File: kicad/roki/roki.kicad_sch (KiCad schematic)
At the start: 64 parts, among them SW1 RotaryEncoder_Switch, SW2 SW_SPDT, U1 Nice_Nano_V2

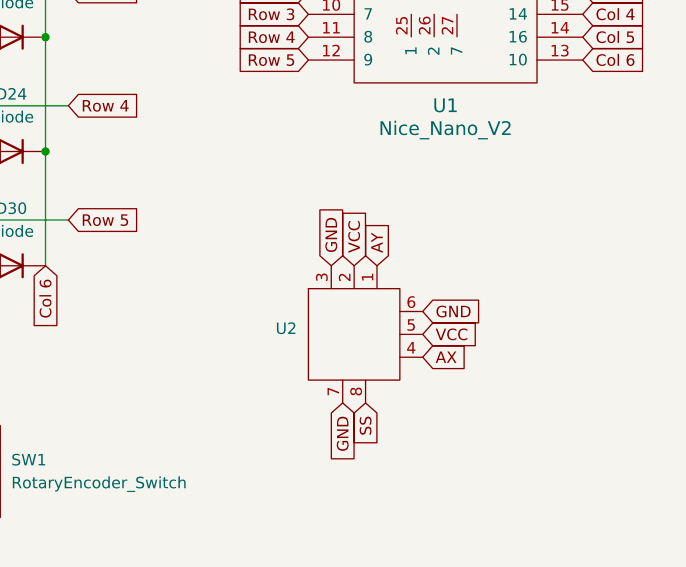
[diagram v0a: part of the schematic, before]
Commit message: fix(kicad): fix thumb stick pin schematics
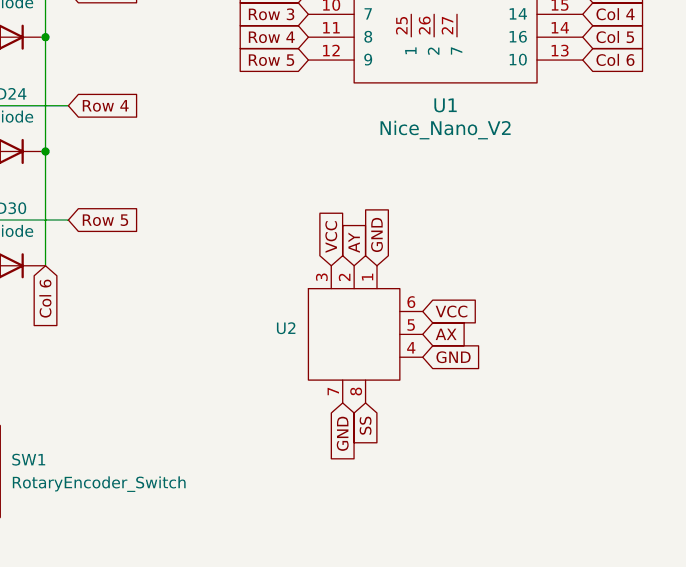
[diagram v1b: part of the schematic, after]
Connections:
- net AX: now also U2.5; no longer U2.4
- net AY: now also U2.2; no longer U2.1
- net GND: now also U2.1, U2.4; no longer U2.3, U2.6
- net VCC: now also U2.3, U2.6; no longer U2.2, U2.5

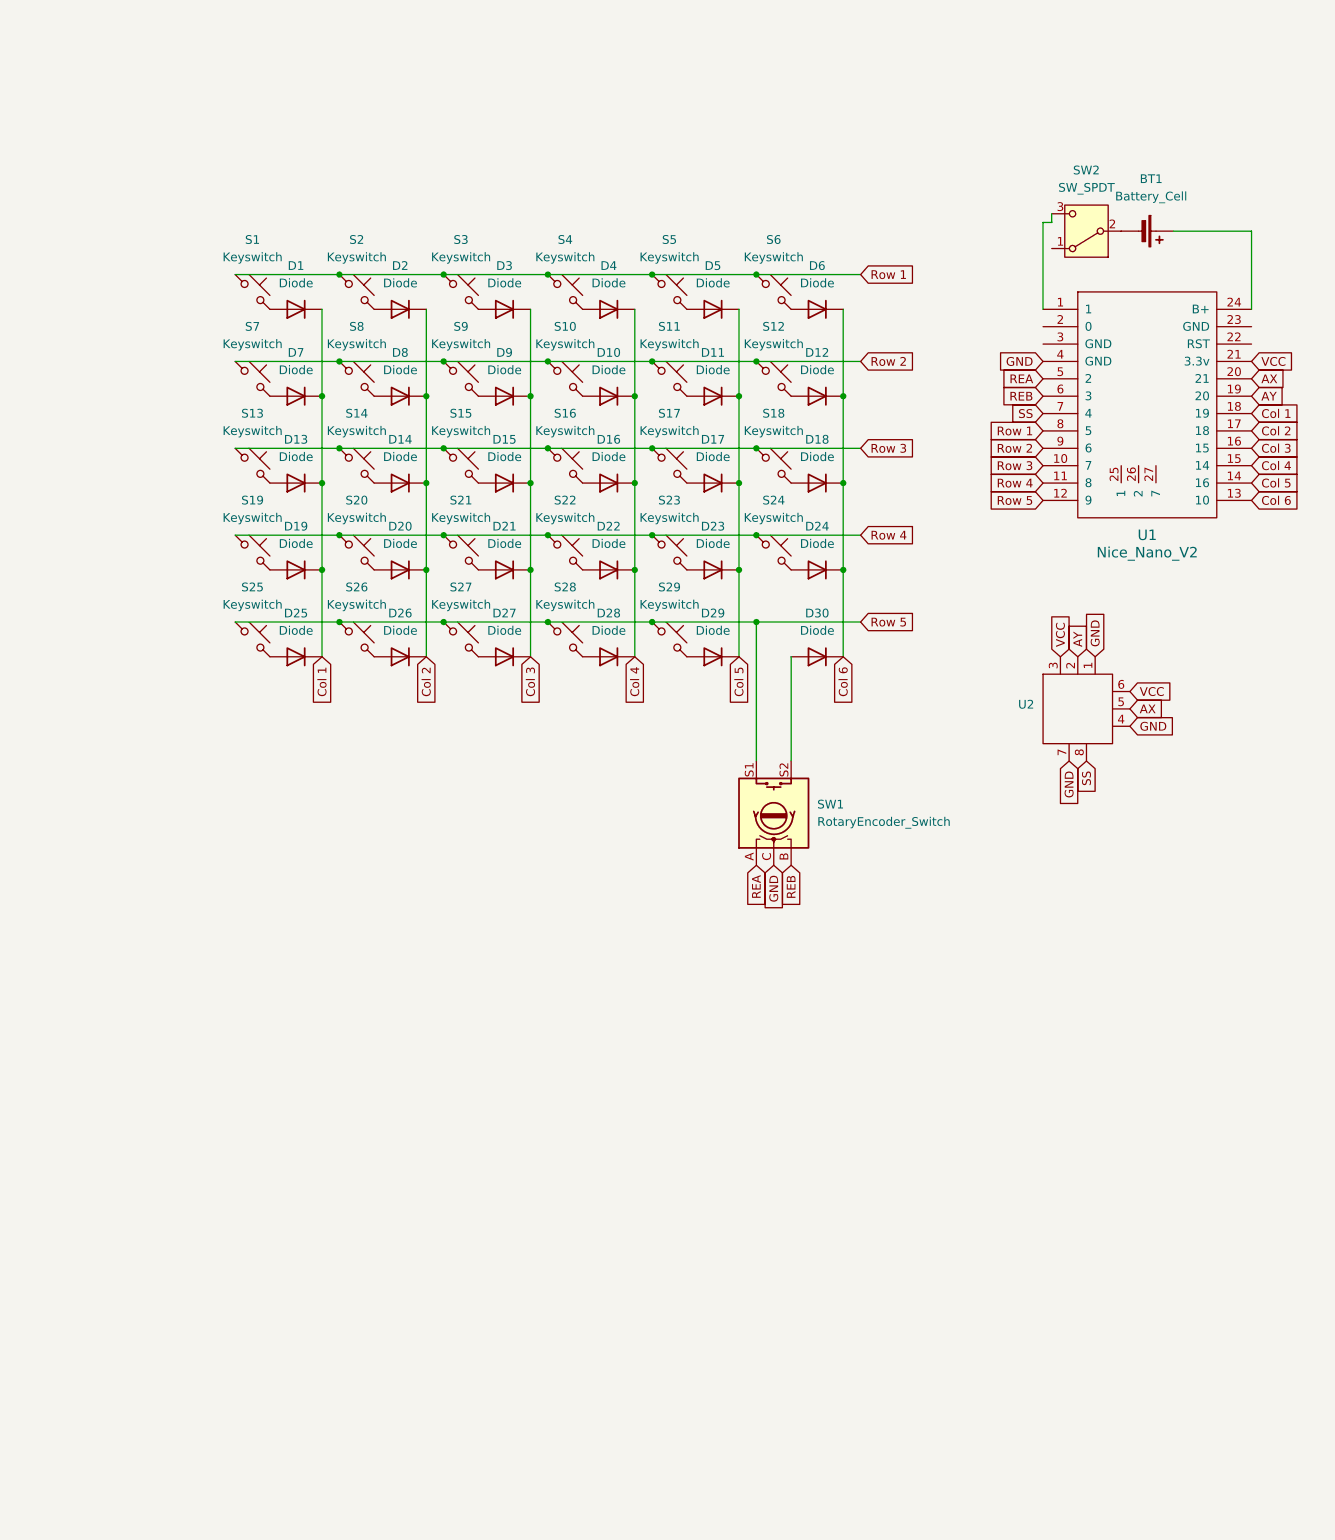
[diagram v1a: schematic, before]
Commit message: feat(kicad): add right side
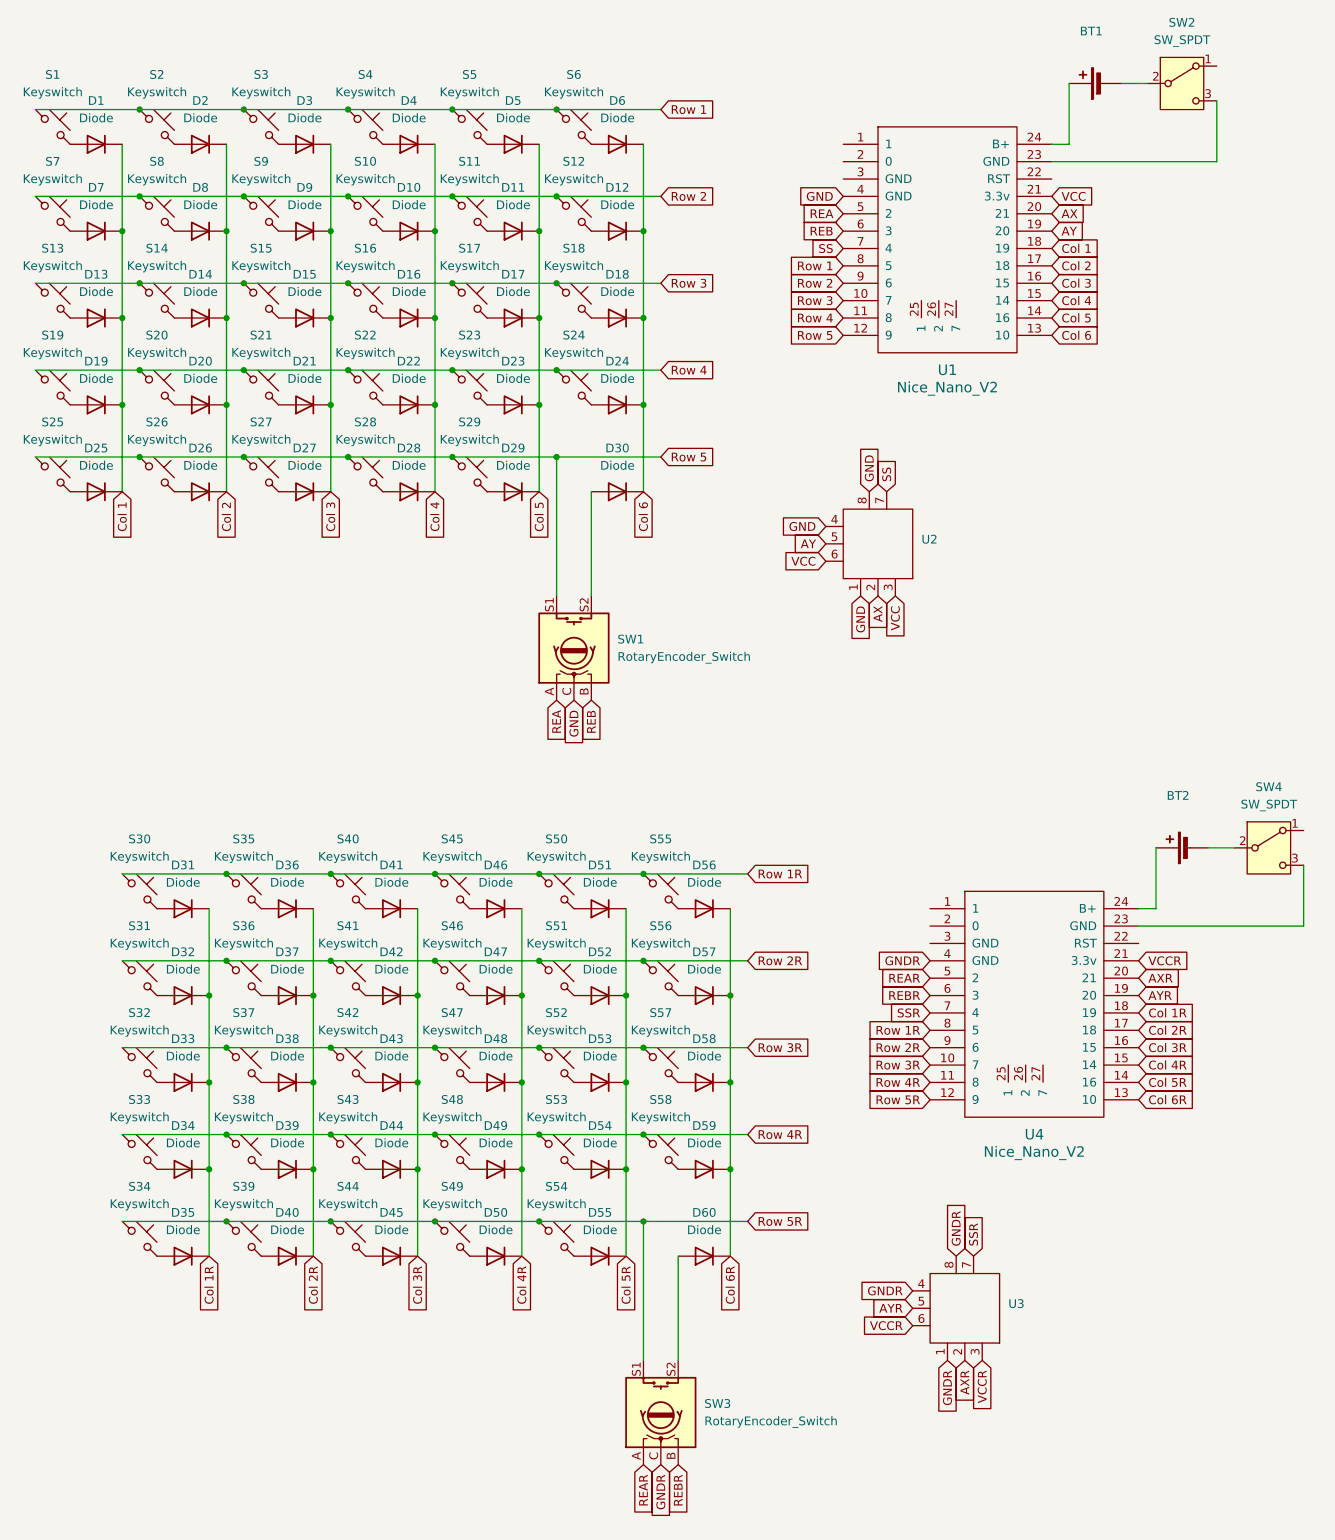
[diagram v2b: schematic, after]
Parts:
- added BT2: Battery_Cell, Battery:BatteryHolder_MPD_BH-18650-PC2, symbol Device:Battery_Cell
- added D31, D32, D33, D34, D35, D36, D37, D38, D39, D40, D41, D42, D43, D44, D45, D46, D47, D48, D49, D50, D51, D52, D53, D54, D55, D56, D57, D58, D59, D60: Diode, ScottoKeebs_Components:Diode_SOD-123, symbol ScottoKeebs:Placeholder_Diode
- added S30, S31, S32, S33, S34, S35, S36, S37, S38, S39, S40, S41, S42, S43, S44, S45, S46, S47, S48, S49, S50, S51, S52, S53, S54, S55, S56, S57, S58: Keyswitch, ScottoKeebs_Hotswap:Hotswap_MX_1.00u, symbol ScottoKeebs:Placeholder_Keyswitch
- added SW3: RotaryEncoder_Switch, Rotary_Encoder:RotaryEncoder_Alps_EC11E-Switch_Vertical_H20mm, symbol Device:RotaryEncoder_Switch
- added SW4: SW_SPDT, Button_Switch_SMD:SW_SPDT_PCM12, symbol Switch:SW_SPDT
- added U3: ~, Library:thumb_stick, symbol Library:thumb_stick
- added U4: Nice_Nano_V2, ScottoKeebs_MCU:Nice_Nano_V2, symbol ScottoKeebs:MCU_Nice_Nano_V2
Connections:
- net AX: now also U2.2; no longer U2.5
- net AY: now also U2.5; no longer U2.2
- net GND: now also U2.8; no longer U2.7
- net SS: now also U2.7; no longer U2.8
- net at U1.1: no longer SW2.3 (C)
- net at U1.23 (GND): now also SW2.3 (C)
- new net: D52.2 (A), S51.2
- new net: D43.2 (A), S42.2
- new net: D50.2 (A), S49.2
- new net: D42.2 (A), S41.2
- new net: D56.2 (A), S55.2
- new net: D55.2 (A), S54.2
- new net: BT2.1 (+), U4.24 (B+)
- new net: BT2.2 (-), SW4.2 (B)
- new net: D49.2 (A), S48.2
- new net: D41.2 (A), S40.2
- new net: D33.2 (A), S32.2
- new net: D44.2 (A), S43.2
- new net: D34.2 (A), S33.2
- new net: D48.2 (A), S47.2
- new net: D37.2 (A), S36.2
- new net: D59.2 (A), S58.2
- new net: D58.2 (A), S57.2
- new net: D46.2 (A), S45.2
- new net: D45.2 (A), S44.2
- new net: D47.2 (A), S46.2
- new net: D38.2 (A), S37.2
- new net: D57.2 (A), S56.2
- new net: D39.2 (A), S38.2
- new net: D31.2 (A), S30.2
- new net: D32.2 (A), S31.2
- new net: D51.2 (A), S50.2
- new net: D35.2 (A), S34.2
- new net: D53.2 (A), S52.2
- new net: D36.2 (A), S35.2
- new net: SW4.3 (C), U4.23 (GND)
- new net: D60.2 (A), SW3.S2
- new net: D54.2 (A), S53.2
- new net: D40.2 (A), S39.2
- new net AXR: U3.2, U4.20 (21)
- new net AYR: U3.5, U4.19 (20)
- new net Col 1R: D31.1 (K), D32.1 (K), D33.1 (K), D34.1 (K), D35.1 (K), U4.18 (19)
- new net Col 2R: D36.1 (K), D37.1 (K), D38.1 (K), D39.1 (K), D40.1 (K), U4.17 (18)
- new net Col 3R: D41.1 (K), D42.1 (K), D43.1 (K), D44.1 (K), D45.1 (K), U4.16 (15)
- new net Col 4R: D46.1 (K), D47.1 (K), D48.1 (K), D49.1 (K), D50.1 (K), U4.15 (14)
- new net Col 5R: D51.1 (K), D52.1 (K), D53.1 (K), D54.1 (K), D55.1 (K), U4.14 (16)
- new net Col 6R: D56.1 (K), D57.1 (K), D58.1 (K), D59.1 (K), D60.1 (K), U4.13 (10)
- new net GNDR: SW3.C, U3.1, U3.4, U3.8, U4.4 (GND)
- new net REAR: SW3.A, U4.5 (2)
- new net REBR: SW3.B, U4.6 (3)
- new net Row 1R: S30.1, S35.1, S40.1, S45.1, S50.1, S55.1, U4.8 (5)
- new net Row 2R: S31.1, S36.1, S41.1, S46.1, S51.1, S56.1, U4.9 (6)
- new net Row 3R: S32.1, S37.1, S42.1, S47.1, S52.1, S57.1, U4.10 (7)
- new net Row 4R: S33.1, S38.1, S43.1, S48.1, S53.1, S58.1, U4.11 (8)
- new net Row 5R: S34.1, S39.1, S44.1, S49.1, S54.1, SW3.S1, U4.12 (9)
- new net SSR: U3.7, U4.7 (4)
- new net VCCR: U3.3, U3.6, U4.21 (3.3v)
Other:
- moved on the sheet: BT1, D1, D10, D11, D12, D13, D14, D15, D16, D17, D18, D19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

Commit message: feat(kicad): update pcb
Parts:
- added BZ1, BZ2: Buzzer, Buzzer_Beeper:Buzzer_TDK_PS1240P02BT_D12.2mm_H6.5mm, symbol Device:Buzzer
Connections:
- net GND: now also BZ1.2 (-)
- net GNDR: now also BZ2.2 (-)
- net BUZZ: now reaches U1.1
- net BUZZ: now also BZ1.1 (+)
- net at SW4.1 (A): now also U4.23 (GND)
- net at SW4.3 (C): no longer U4.23 (GND)
- net BUZZR: now reaches U4.1
- net BUZZR: now also BZ2.1 (+)

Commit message: feat(kicad): update pcb
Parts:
- renumbered D36 to D32, D41 to D33, D46 to D34, D51 to D35, D56 to D36, D32 to D37, D37 to D38, D42 to D39, D47 to D40, D52 to D41, D57 to D42, D33 to D43, D38 to D44, D43 to D45, D48 to D46, D53 to D47, D58 to D48, D34 to D49, D39 to D50, D44 to D51, D49 to D52, D54 to D53, D59 to D54, D35 to D55, D40 to D56, D45 to D57, D50 to D58, D55 to D59, S35 to S31, S40 to S32, S45 to S33, S50 to S34, S55 to S35, S31 to S36, S36 to S37, S41 to S38, S46 to S39, S51 to S40, S56 to S41, S32 to S42, S37 to S43, S42 to S44, S47 to S45, S52 to S46, S57 to S47, S33 to S48, S38 to S49, S43 to S50, S48 to S51, S53 to S52, S58 to S53, S34 to S54, S39 to S55, S44 to S56, S49 to S57, S54 to S58
